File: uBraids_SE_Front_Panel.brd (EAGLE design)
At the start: 40.3 x 128.5 mm, 3 parts

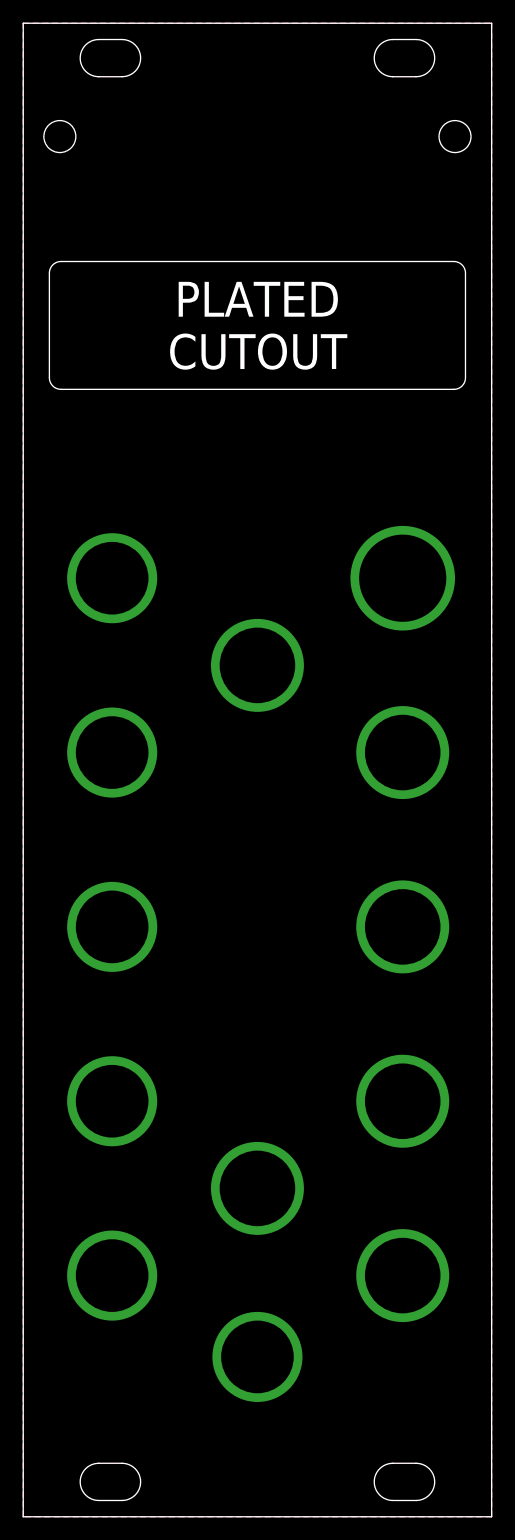
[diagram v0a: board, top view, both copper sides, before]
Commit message: revision C first pass, primarily to address rail clearance
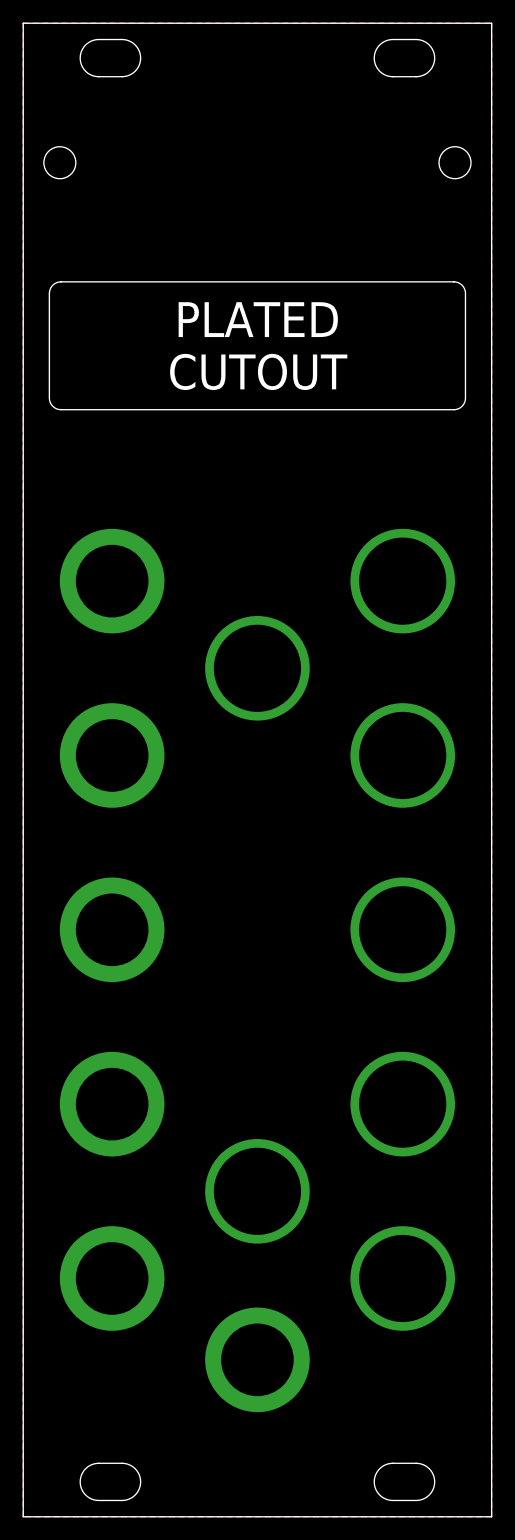
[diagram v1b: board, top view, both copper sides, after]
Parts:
- moved E$1 3.00 mm to (22.5, 111.0)
- moved E$3 0.50 mm to (32.6, 11.5)
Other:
- outline, holes or cut-outs redrawn
- board text added: "Dervied from work by: Olivier Gillet of Mutable Instruments, Magpie Modular, and Neutron Sound"
- board text added: "TALL-DOG.COM 2017-10-23 REV-C"
- board text added: "TD-UBSE-C"
- board text removed: "Panel dervied from work by: Mutable Instruments and Magpie Modular"
- board text removed: "TALL-DOG.COM 2017-06-14"

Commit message: removed additional 0.5 mm from main board, adjusted panel to match
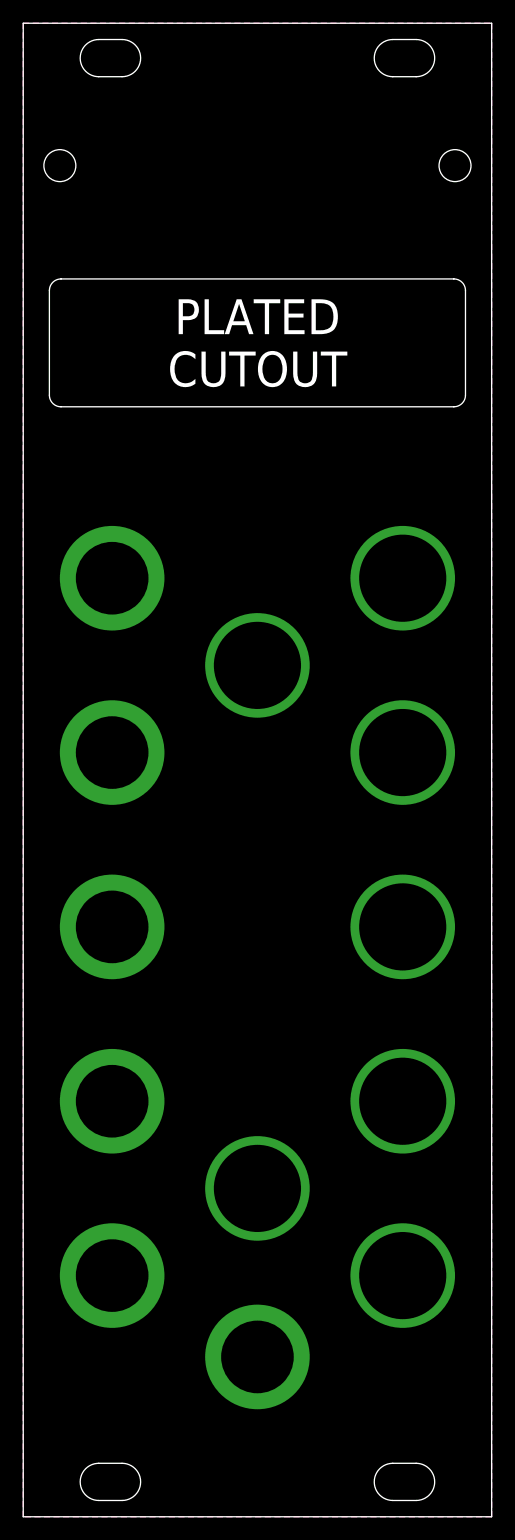
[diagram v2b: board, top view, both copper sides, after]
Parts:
- moved E$1 0.25 mm to (22.5, 111.2)
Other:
- outline, holes or cut-outs redrawn

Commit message: prep for production of revision C
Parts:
- removed E$1: (no value), uBraids_SE:UBRAIDS-SE
- E$3: device uBraids_SE:CC-LOGO -> uBraids_SE:MARKING-CC-LOGO
- moved E$3 0.25 mm to (32.6, 11.8)
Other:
- outline, holes or cut-outs redrawn
- board text added: "Panel dervied from work by: Olivier Gillet of Mutable Instruments, Magpie Modular, and Neutron Sound"
- board text added: "TALL-DOG.COM 2017-10-24 TD-UBSE-C"
- board text removed: "Dervied from work by: Olivier Gillet of Mutable Instruments, Magpie Modular, and Neutron Sound"
- board text removed: "TALL-DOG.COM 2017-10-23 REV-C"
